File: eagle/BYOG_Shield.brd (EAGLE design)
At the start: 71.2 x 64.5 mm, 1 part, among them U1 ARDUINOR3-NOIOREF-NOTEXT

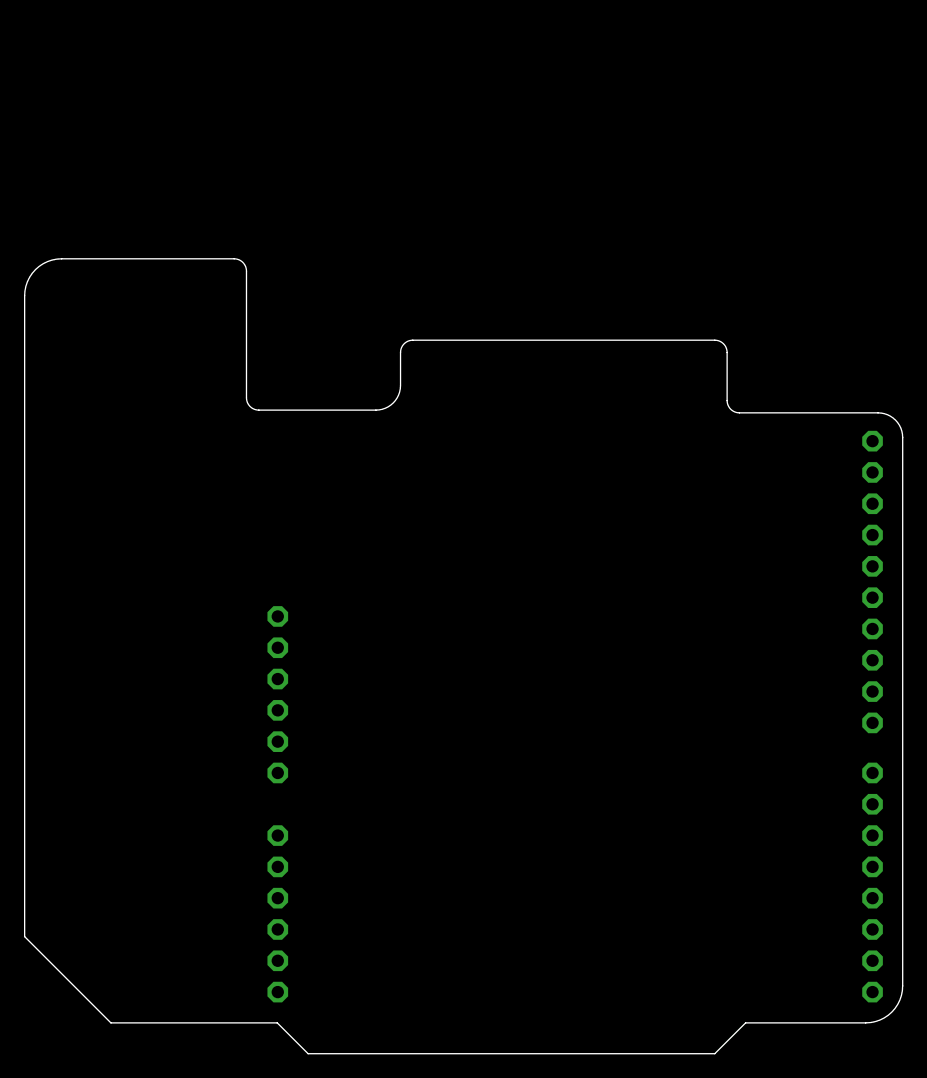
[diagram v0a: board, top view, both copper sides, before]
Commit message: COMPLETE & EXPRESS versions of PCB files added
Added in EXPRESS and COMPLETE version of the EAGLE files to
complete/refer to.
Use EXPRESS to jumpstart the routing task. Good luck and have fun!
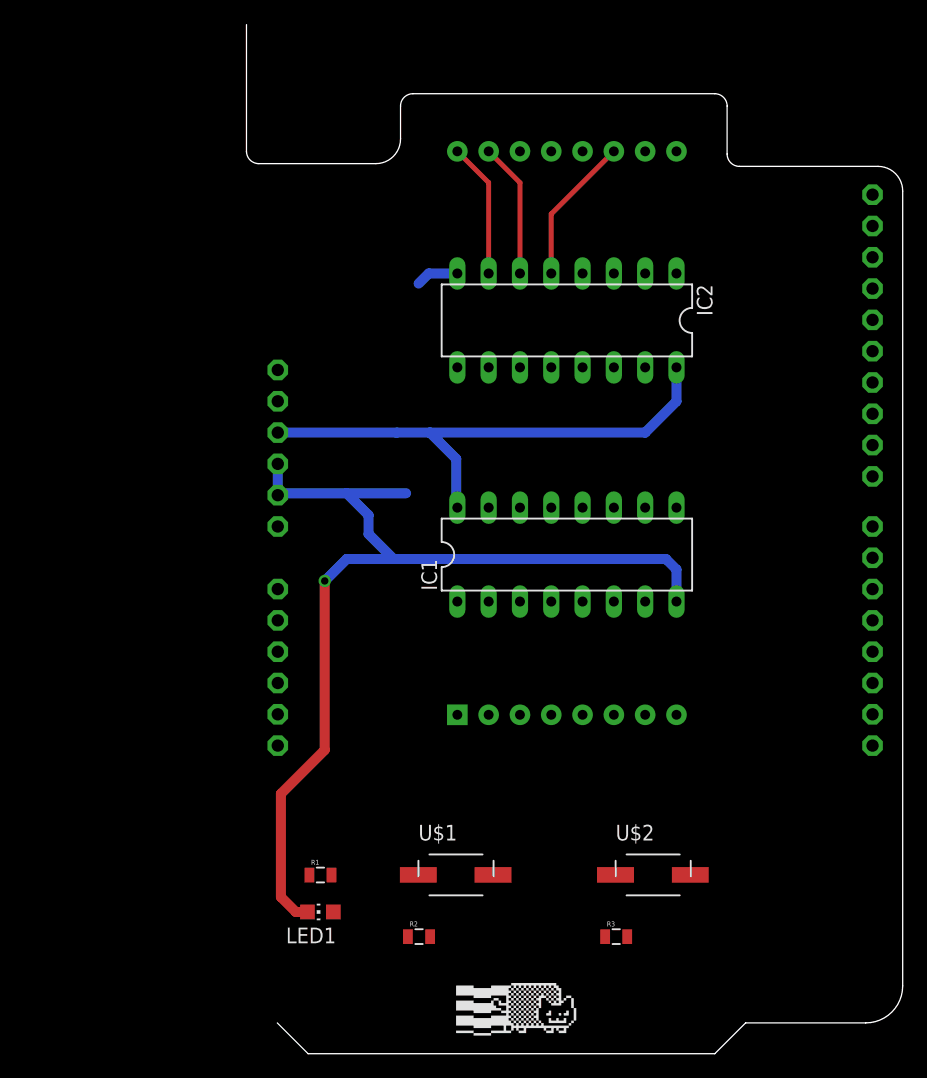
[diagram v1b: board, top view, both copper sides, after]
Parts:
- added IC1, IC2: 74HC595N, AISCube_BYOG:DIL16
- added LED1: (no value), AISCube_BYOG:CHIP-LED0805
- added R1, R2, R3: (no value), AISCube_BYOG:0805
- added U$1, U$2: PB_SMTFITTING, AISCube_BYOG:PB_SMT_TIGHT
- added U$3: 8X8DM_2088AS, AISCube_BYOG:8X8DM_2088AS
- added U$8: (no value), AISCube_BYOG:LOGO_NYAN
- moved U1 20.0 mm to (0.00, 89.0)
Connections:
- removed net GND1: U1.GND1
- removed net GND2: U1.GND2
- new net N$1: R1.1, U1.D10
- new net N$10: IC1.3, U$3.12
- new net N$11: IC1.4, U$3.1
- new net N$12: IC1.5, U$3.7
- new net N$13: IC1.6, U$3.2
- new net N$14: IC1.7, U$3.5
- new net N$15: IC1.15, U$3.9
- new net N$16: IC2.1, U$3.3
- new net N$17: IC2.2, U$3.4
- new net N$18: IC2.3, U$3.10
- new net N$19: IC2.4, U$3.6
- new net N$20: IC2.5, U$3.11
- new net N$21: IC2.6, U$3.15
- new net N$22: IC2.7, U$3.16
- new net N$23: IC2.15, U$3.13
- new net N$5: LED1.A, R1.2
- new net N$6: R2.1, U$1.P$3
- new net N$7: R3.1, U$2.P$3
- new net N$8: IC1.1, U$3.14
- new net N$9: IC1.2, U$3.8
- new net PB1: U1.D5
- new net PB2: U1.D6
- net 5V: now also IC1.16, IC2.16, R2.2, R3.2
- net GND: now also IC1.8, IC2.8, LED1.C, U1.GND1, U1.GND2
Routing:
- net GND: track 0.00 -> 85.4 mm, vias 0 -> 1
- net 5V: track 0.00 -> 43.2 mm
- net N$20: track 0.00 -> 12.0 mm
- net N$21: track 0.00 -> 11.0 mm
- net N$22: track 0.00 -> 11.0 mm
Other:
- board size 71.2 x 64.5 mm -> 53.2 x 83.5 mm
